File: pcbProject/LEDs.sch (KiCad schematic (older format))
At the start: 10 parts

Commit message: deel1routingpcb
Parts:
- LED1, LED3, LED4, LED5, LED6: footprint (none) -> LED_SMD:LED_0805_2012Metric
- R10, R6, R7, R8, R9: footprint (none) -> Resistor_SMD:R_1206_3216Metric
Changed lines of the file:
@@
 F 0 "R1" V 4675 3300 50  0000 C CNN
 F 1 "470" V 4509 3125 50  0000 C CNN
-F 2 "" V 4555 3125 50  0001 C CNN
+F 2 "Resistor_SMD:R_1206_3216Metric" V 4555 3125 50  0001 C CNN
 F 3 "~" H 4625 3125 50  0001 C CNN
 	1    4625 3125
@@
 F 0 "R2" V 4675 3600 50  0000 C CNN
 F 1 "470" V 4509 3425 50  0000 C CNN
-F 2 "" V 4555 3425 50  0001 C CNN
+F 2 "Resistor_SMD:R_1206_3216Metric" V 4555 3425 50  0001 C CNN
 F 3 "~" H 4625 3425 50  0001 C CNN
 	1    4625 3425
@@
 F 0 "R3" V 4675 3925 50  0000 C CNN
 F 1 "470" V 4509 3750 50  0000 C CNN
-F 2 "" V 4555 3750 50  0001 C CNN
+F 2 "Resistor_SMD:R_1206_3216Metric" V 4555 3750 50  0001 C CNN
 F 3 "~" H 4625 3750 50  0001 C CNN
 	1    4625 3750
@@
 F 0 "R4" V 4675 4225 50  0000 C CNN
 F 1 "470" V 4509 4050 50  0000 C CNN
-F 2 "" V 4555 4050 50  0001 C CNN
+F 2 "Resistor_SMD:R_1206_3216Metric" V 4555 4050 50  0001 C CNN
 F 3 "~" H 4625 4050 50  0001 C CNN
 	1    4625 4050
@@
 F 0 "LED3" H 4025 3000 50  0000 C CNN
 F 1 "BLUE" H 3850 3200 50  0000 C CNN
-F 2 "" H 4025 3125 60  0001 C CNN
+F 2 "LED_SMD:LED_0805_2012Metric" H 4025 3125 60  0001 C CNN
 F 3 "" H 4025 3125 60  0000 C CNN
 	1    4025 3125
@@
 F 0 "LED4" H 4025 3325 50  0000 C CNN
 F 1 "BLUE" H 3850 3500 50  0000 C CNN
-F 2 "" H 4025 3425 60  0001 C CNN
+F 2 "LED_SMD:LED_0805_2012Metric" H 4025 3425 60  0001 C CNN
 F 3 "" H 4025 3425 60  0000 C CNN
 	1    4025 3425
@@
 F 0 "LED5" H 4025 3650 50  0000 C CNN
 F 1 "BLUE" H 3850 3825 50  0000 C CNN
-F 2 "" H 4025 3750 60  0001 C CNN
+F 2 "LED_SMD:LED_0805_2012Metric" H 4025 3750 60  0001 C CNN
 F 3 "" H 4025 3750 60  0000 C CNN
 	1    4025 3750
@@
 F 0 "LED6" H 4025 3950 50  0000 C CNN
 F 1 "BLUE" H 3850 4125 50  0000 C CNN
-F 2 "" H 4025 4050 60  0001 C CNN
+F 2 "LED_SMD:LED_0805_2012Metric" H 4025 4050 60  0001 C CNN
 F 3 "" H 4025 4050 60  0000 C CNN
 	1    4025 4050
@@
 F 0 "R10" V 4675 2700 50  0000 C CNN
 F 1 "470" V 4509 2525 50  0000 C CNN
-F 2 "" V 4555 2525 50  0001 C CNN
+F 2 "Resistor_SMD:R_1206_3216Metric" V 4555 2525 50  0001 C CNN
 F 3 "~" H 4625 2525 50  0001 C CNN
 	1    4625 2525
@@
 F 0 "LED1" H 4025 2400 50  0000 C CNN
 F 1 "GREEN" H 3850 2600 50  0000 C CNN
-F 2 "" H 4025 2525 60  0001 C CNN
+F 2 "LED_SMD:LED_0805_2012Metric" H 4025 2525 60  0001 C CNN
 F 3 "" H 4025 2525 60  0000 C CNN
 	1    4025 2525

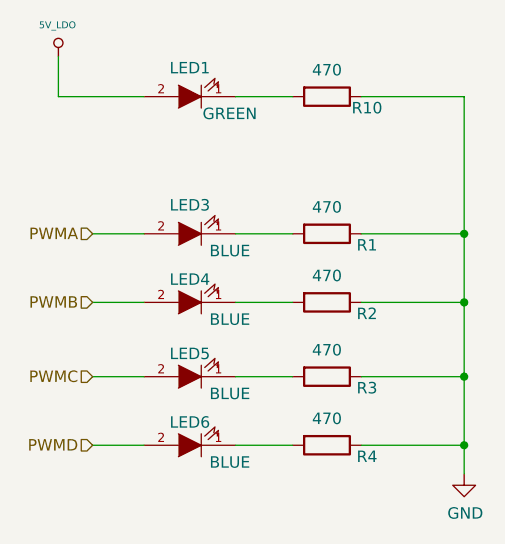
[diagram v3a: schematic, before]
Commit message: PCB versie3
Aanpassingen tips coach --> veel gewijzigd
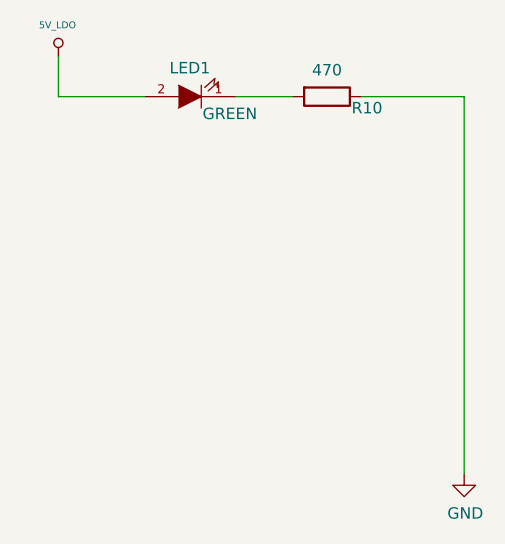
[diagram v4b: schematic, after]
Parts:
- removed LED3, LED4, LED5, LED6: BLUE, LED_SMD:LED_0805_2012Metric, symbol Arduino_Uno_R3_From_Scratch-rescue:LED
- removed R6, R7, R8, R9: 470, Resistor_SMD:R_1206_3216Metric, symbol Device:R
- R10: footprint Resistor_SMD:R_1206_3216Metric -> Resistor_SMD:R_1206_3216Metric_Pad1.42x1.75mm_HandSolder
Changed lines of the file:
@@
 $EndDescr
-$Comp
-L Device:R R9
-U 1 1 5C6D94A2
-P 4625 3125
-AR Path="/5BE519F1/5C6D94A2" Ref="R9"  Part="1"
-AR Path="/5C6DA90A/5C6D94A2" Ref="R1"  Part="1"
-AR Path="/5C6DD8AC/5C6D94A2" Ref="R?"  Part="1"
-F 0 "R1" V 4675 3300 50  0000 C CNN
-F 1 "470" V 4509 3125 50  0000 C CNN
-F 2 "Resistor_SMD:R_1206_3216Metric" V 4555 3125 50  0001 C CNN
-F 3 "~" H 4625 3125 50  0001 C CNN
-	1    4625 3125
-	0    1    1    0
-$EndComp
-$Comp
-L Device:R R8
-U 1 1 5C78928C
-P 4625 3425
-AR Path="/5BE519F1/5C78928C" Ref="R8"  Part="1"
-AR Path="/5C6DA90A/5C78928C" Ref="R2"  Part="1"
-AR Path="/5C6DD8AC/5C78928C" Ref="R?"  Part="1"
-F 0 "R2" V 4675 3600 50  0000 C CNN
-F 1 "470" V 4509 3425 50  0000 C CNN
-F 2 "Resistor_SMD:R_1206_3216Metric" V 4555 3425 50  0001 C CNN
-F 3 "~" H 4625 3425 50  0001 C CNN
-	1    4625 3425
-	0    1    1    0
-$EndComp
-$Comp
-L Device:R R7
-U 1 1 5C78928D
-P 4625 3750
-AR Path="/5BE519F1/5C78928D" Ref="R7"  Part="1"
-AR Path="/5C6DA90A/5C78928D" Ref="R3"  Part="1"
-AR Path="/5C6DD8AC/5C78928D" Ref="R?"  Part="1"
-F 0 "R3" V 4675 3925 50  0000 C CNN
-F 1 "470" V 4509 3750 50  0000 C CNN
-F 2 "Resistor_SMD:R_1206_3216Metric" V 4555 3750 50  0001 C CNN
-F 3 "~" H 4625 3750 50  0001 C CNN
-	1    4625 3750
-	0    1    1    0
-$EndComp
-$Comp
-L Device:R R6
-U 1 1 5C78928E
-P 4625 4050
-AR Path="/5BE519F1/5C78928E" Ref="R6"  Part="1"
-AR Path="/5C6DA90A/5C78928E" Ref="R4"  Part="1"
-AR Path="/5C6DD8AC/5C78928E" Ref="R?"  Part="1"
-F 0 "R4" V 4675 4225 50  0000 C CNN
-F 1 "470" V 4509 4050 50  0000 C CNN
-F 2 "Resistor_SMD:R_1206_3216Metric" V 4555 4050 50  0001 C CNN
-F 3 "~" H 4625 4050 50  0001 C CNN
-	1    4625 4050
-	0    1    1    0
-$EndComp
-Text HLabel 3600 3125 0    50   Input ~ 0
-PWMA
-Text HLabel 3600 3425 0    50   Input ~ 0
-PWMB
-Text HLabel 3600 3750 0    50   Input ~ 0
-PWMC
-Text HLabel 3600 4050 0    50   Input ~ 0
-PWMD
-Wire Wire Line
-	5225 3125 4775 3125
-Wire Wire Line
-	5225 3125 5225 3425
-Wire Wire Line
-	5225 3425 4775 3425
-Wire Wire Line
-	5225 3425 5225 3750
-Wire Wire Line
-	5225 3750 4775 3750
-Connection ~ 5225 3425
-Wire Wire Line
-	5225 3750 5225 4050
-Wire Wire Line
-	5225 4050 4775 4050
-Connection ~ 5225 3750
 $Comp
 L power:GND #PWR0103
@@
 	1    0    0    -1
 $EndComp
-Wire Wire Line
-	5225 4175 5225 4050
-Connection ~ 5225 4050
-$Comp
-L Arduino_Uno_R3_From_Scratch-rescue:LED LED3
-U 1 1 5C6DB0B8
-P 4025 3125
-AR Path="/5C6DA90A/5C6DB0B8" Ref="LED3"  Part="1"
-AR Path="/5C6DD8AC/5C6DB0B8" Ref="LED?"  Part="1"
-F 0 "LED3" H 4025 3000 50  0000 C CNN
-F 1 "BLUE" H 3850 3200 50  0000 C CNN
-F 2 "LED_SMD:LED_0805_2012Metric" H 4025 3125 60  0001 C CNN
-F 3 "" H 4025 3125 60  0000 C CNN
-	1    4025 3125
-	-1   0    0    1
-$EndComp
-$Comp
-L Arduino_Uno_R3_From_Scratch-rescue:LED LED4
-U 1 1 5C6DB14A
-P 4025 3425
-AR Path="/5C6DA90A/5C6DB14A" Ref="LED4"  Part="1"
-AR Path="/5C6DD8AC/5C6DB14A" Ref="LED?"  Part="1"
-F 0 "LED4" H 4025 3325 50  0000 C CNN
-F 1 "BLUE" H 3850 3500 50  0000 C CNN
-F 2 "LED_SMD:LED_0805_2012Metric" H 4025 3425 60  0001 C CNN
-F 3 "" H 4025 3425 60  0000 C CNN
-	1    4025 3425
-	-1   0    0    1
-$EndComp
-$Comp
-L Arduino_Uno_R3_From_Scratch-rescue:LED LED5
-U 1 1 5C6DB254
-P 4025 3750
-AR Path="/5C6DA90A/5C6DB254" Ref="LED5"  Part="1"
-AR Path="/5C6DD8AC/5C6DB254" Ref="LED?"  Part="1"
-F 0 "LED5" H 4025 3650 50  0000 C CNN
-F 1 "BLUE" H 3850 3825 50  0000 C CNN
-F 2 "LED_SMD:LED_0805_2012Metric" H 4025 3750 60  0001 C CNN
-F 3 "" H 4025 3750 60  0000 C CNN
-	1    4025 3750
-	-1   0    0    1
-$EndComp
-$Comp
-L Arduino_Uno_R3_From_Scratch-rescue:LED LED6
-U 1 1 5C6DB25B
-P 4025 4050
-AR Path="/5C6DA90A/5C6DB25B" Ref="LED6"  Part="1"
-AR Path="/5C6DD8AC/5C6DB25B" Ref="LED?"  Part="1"
-F 0 "LED6" H 4025 3950 50  0000 C CNN
-F 1 "BLUE" H 3850 4125 50  0000 C CNN
-F 2 "LED_SMD:LED_0805_2012Metric" H 4025 4050 60  0001 C CNN
-F 3 "" H 4025 4050 60  0000 C CNN
-	1    4025 4050
-	-1   0    0    1
-$EndComp
-Wire Wire Line
-	3600 3125 3825 3125
-Wire Wire Line
-	3600 3425 3825 3425
-Wire Wire Line
-	4225 3425 4475 3425
-Wire Wire Line
-	3600 3750 3825 3750
-Wire Wire Line
-	4225 3750 4475 3750
-Wire Wire Line
-	3600 4050 3825 4050
-Wire Wire Line
-	4225 4050 4475 4050
-Wire Wire Line
-	4225 3125 4475 3125
 $Comp
 L Device:R R?
@@
 F 0 "R10" V 4675 2700 50  0000 C CNN
 F 1 "470" V 4509 2525 50  0000 C CNN
-F 2 "Resistor_SMD:R_1206_3216Metric" V 4555 2525 50  0001 C CNN
+F 2 "Resistor_SMD:R_1206_3216Metric_Pad1.42x1.75mm_HandSolder" V 4555 2525 50  0001 C CNN
 F 3 "~" H 4625 2525 50  0001 C CNN
 	1    4625 2525
@@
 Wire Wire Line
 	4225 2525 4475 2525
-Wire Wire Line
-	5225 2525 5225 3125
-Connection ~ 5225 3125
 $Comp
 L Arduino_Uno_R3_From_Scratch:5V_LDO #PWR0104
@@
 Wire Wire Line
 	3450 2525 3825 2525
+Wire Wire Line
+	5225 2525 5225 4175
 $EndSCHEMATC

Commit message: verslag
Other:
- moved on the sheet: LED1, R10
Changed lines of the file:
@@
 $Descr A4 11693 8268
 encoding utf-8
-Sheet 11 11
+Sheet 10 11
 Title ""
 Date ""
@@
 $EndDescr
 $Comp
-L power:GND #PWR0103
-U 1 1 5C6DAF20
-P 5225 4175
-AR Path="/5C6DA90A/5C6DAF20" Ref="#PWR0103"  Part="1"
-AR Path="/5C6DD8AC/5C6DAF20" Ref="#PWR?"  Part="1"
-F 0 "#PWR0103" H 5225 3925 50  0001 C CNN
-F 1 "GND" H 5230 4002 50  0000 C CNN
-F 2 "" H 5225 4175 50  0001 C CNN
-F 3 "" H 5225 4175 50  0001 C CNN
-	1    5225 4175
-	1    0    0    -1
-$EndComp
-$Comp
 L Device:R R?
 U 1 1 5C6DCC06
-P 4625 2525
+P 3450 3125
 AR Path="/5BE519F1/5C6DCC06" Ref="R?"  Part="1"
 AR Path="/5C6DA90A/5C6DCC06" Ref="R10"  Part="1"
 AR Path="/5C6DD8AC/5C6DCC06" Ref="R?"  Part="1"
-F 0 "R10" V 4675 2700 50  0000 C CNN
-F 1 "470" V 4509 2525 50  0000 C CNN
-F 2 "Resistor_SMD:R_1206_3216Metric_Pad1.42x1.75mm_HandSolder" V 4555 2525 50  0001 C CNN
-F 3 "~" H 4625 2525 50  0001 C CNN
-	1    4625 2525
-	0    1    1    0
+F 0 "R10" V 3550 3125 50  0000 C CNN
+F 1 "470" V 3334 3125 50  0000 C CNN
+F 2 "Resistor_SMD:R_1206_3216Metric_Pad1.42x1.75mm_HandSolder" V 3380 3125 50  0001 C CNN
+F 3 "~" H 3450 3125 50  0001 C CNN
+	1    3450 3125
+	-1   0    0    1
 $EndComp
-Wire Wire Line
-	5225 2525 4775 2525
 $Comp
 L Arduino_Uno_R3_From_Scratch-rescue:LED LED1
 U 1 1 5C6DCC0F
-P 4025 2525
+P 3450 2725
 AR Path="/5C6DA90A/5C6DCC0F" Ref="LED1"  Part="1"
 AR Path="/5C6DD8AC/5C6DCC0F" Ref="LED?"  Part="1"
-F 0 "LED1" H 4025 2400 50  0000 C CNN
-F 1 "GREEN" H 3850 2600 50  0000 C CNN
-F 2 "LED_SMD:LED_0805_2012Metric" H 4025 2525 60  0001 C CNN
-F 3 "" H 4025 2525 60  0000 C CNN
-	1    4025 2525
-	-1   0    0    1
+F 0 "LED1" H 3450 2600 50  0000 C CNN
+F 1 "GREEN" H 3425 2850 50  0000 C CNN
+F 2 "LED_SMD:LED_0805_2012Metric" H 3450 2725 60  0001 C CNN
+F 3 "" H 3450 2725 60  0000 C CNN
+	1    3450 2725
+	0    -1   -1   0
 $EndComp
-Wire Wire Line
-	4225 2525 4475 2525
 $Comp
 L Arduino_Uno_R3_From_Scratch:5V_LDO #PWR0104
@@
 Wire Wire Line
 	3450 2350 3450 2525
+$Comp
+L power:GND #PWR0103
+U 1 1 5C6DAF20
+P 3450 3350
+AR Path="/5C6DA90A/5C6DAF20" Ref="#PWR0103"  Part="1"
+AR Path="/5C6DD8AC/5C6DAF20" Ref="#PWR?"  Part="1"
+F 0 "#PWR0103" H 3450 3100 50  0001 C CNN
+F 1 "GND" H 3455 3177 50  0000 C CNN
+F 2 "" H 3450 3350 50  0001 C CNN
+F 3 "" H 3450 3350 50  0001 C CNN
+	1    3450 3350
+	1    0    0    -1
+$EndComp
 Wire Wire Line
-	3450 2525 3825 2525
+	3450 3350 3450 3275
 Wire Wire Line
-	5225 2525 5225 4175
+	3450 2975 3450 2925
 $EndSCHEMATC
